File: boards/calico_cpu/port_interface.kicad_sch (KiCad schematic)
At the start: 30 parts, among them J3 Conn_02x06_Top_Bottom, J4 Conn_02x06_Top_Bottom, U58 74HC126, U59 74HC126, U60 74HC126, U61 74HC126, U62 74HC273, U63 74HC273

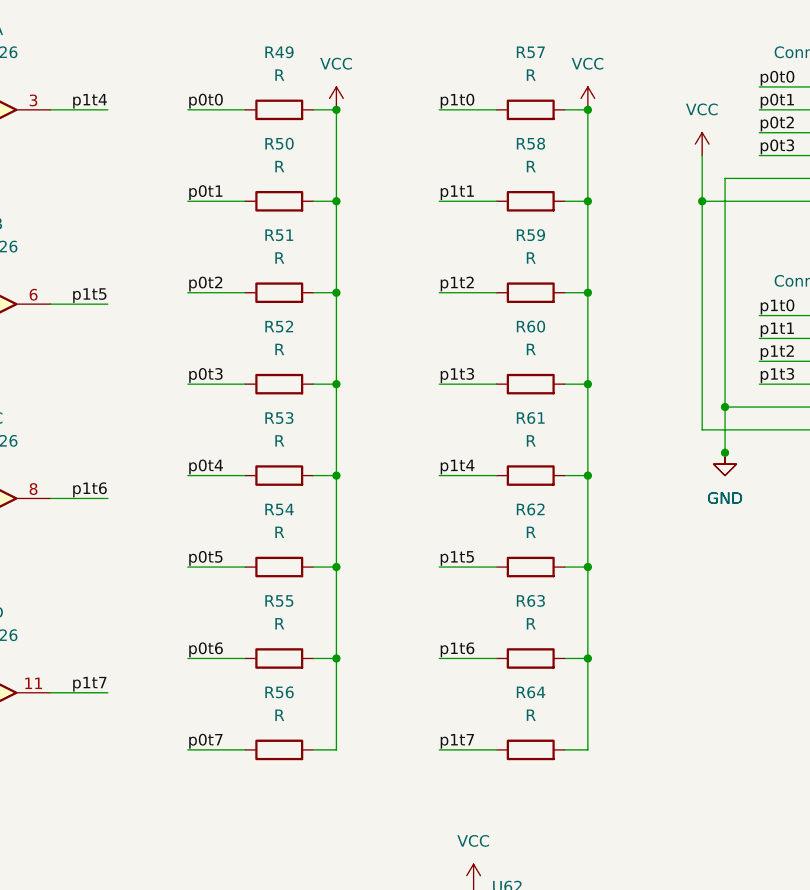
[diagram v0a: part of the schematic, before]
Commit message: set LED and resistors
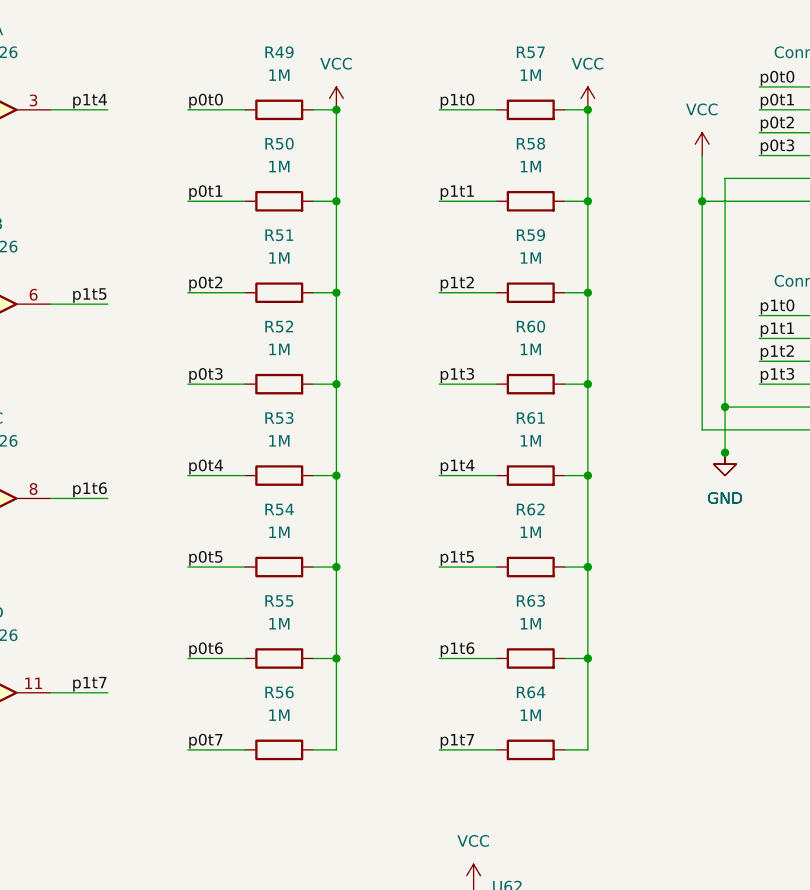
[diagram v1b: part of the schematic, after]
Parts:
- R49, R50, R51, R52, R53, R54, R55, R56, R57, R58, R59, R60, R61, R62, R63, R64: value R -> 1M
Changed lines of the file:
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@@
     (in_bom yes) (on_board yes) (fields_autoplaced)
     (property "Reference" "R57" (id 0) (at 215.9 22.86 90))
-    (property "Value" "R" (id 1) (at 215.9 25.4 90))
+    (property "Value" "1M" (id 1) (at 215.9 25.4 90))
     (property "Footprint" "Resistor_SMD:R_0805_2012Metric_Pad1.20x1.40mm_HandSolder" (id 2) (at 215.9 30.988 90)
       (effects (font (size 1.27 1.27)) hide)
@@
     (in_bom yes) (on_board yes) (fields_autoplaced)
     (property "Reference" "R53" (id 0) (at 187.96 63.5 90))
-    (property "Value" "R" (id 1) (at 187.96 66.04 90))
+    (property "Value" "1M" (id 1) (at 187.96 66.04 90))
     (property "Footprint" "Resistor_SMD:R_0805_2012Metric_Pad1.20x1.40mm_HandSolder" (id 2) (at 187.96 71.628 90)
       (effects (font (size 1.27 1.27)) hide)
@@
     (in_bom yes) (on_board yes) (fields_autoplaced)
     (property "Reference" "R60" (id 0) (at 215.9 53.34 90))
-    (property "Value" "R" (id 1) (at 215.9 55.88 90))
+    (property "Value" "1M" (id 1) (at 215.9 55.88 90))
     (property "Footprint" "Resistor_SMD:R_0805_2012Metric_Pad1.20x1.40mm_HandSolder" (id 2) (at 215.9 61.468 90)
       (effects (font (size 1.27 1.27)) hide)
@@
     (in_bom yes) (on_board yes) (fields_autoplaced)
     (property "Reference" "R49" (id 0) (at 187.96 22.86 90))
-    (property "Value" "R" (id 1) (at 187.96 25.4 90))
+    (property "Value" "1M" (id 1) (at 187.96 25.4 90))
     (property "Footprint" "Resistor_SMD:R_0805_2012Metric_Pad1.20x1.40mm_HandSolder" (id 2) (at 187.96 30.988 90)
       (effects (font (size 1.27 1.27)) hide)
@@
     (in_bom yes) (on_board yes) (fields_autoplaced)
     (property "Reference" "R59" (id 0) (at 215.9 43.18 90))
-    (property "Value" "R" (id 1) (at 215.9 45.72 90))
+    (property "Value" "1M" (id 1) (at 215.9 45.72 90))
     (property "Footprint" "Resistor_SMD:R_0805_2012Metric_Pad1.20x1.40mm_HandSolder" (id 2) (at 215.9 51.308 90)
       (effects (font (size 1.27 1.27)) hide)
@@
     (in_bom yes) (on_board yes) (fields_autoplaced)
     (property "Reference" "R61" (id 0) (at 215.9 63.5 90))
-    (property "Value" "R" (id 1) (at 215.9 66.04 90))
+    (property "Value" "1M" (id 1) (at 215.9 66.04 90))
     (property "Footprint" "Resistor_SMD:R_0805_2012Metric_Pad1.20x1.40mm_HandSolder" (id 2) (at 215.9 71.628 90)
       (effects (font (size 1.27 1.27)) hide)
@@
     (in_bom yes) (on_board yes) (fields_autoplaced)
     (property "Reference" "R62" (id 0) (at 215.9 73.66 90))
-    (property "Value" "R" (id 1) (at 215.9 76.2 90))
+    (property "Value" "1M" (id 1) (at 215.9 76.2 90))
     (property "Footprint" "Resistor_SMD:R_0805_2012Metric_Pad1.20x1.40mm_HandSolder" (id 2) (at 215.9 81.788 90)
       (effects (font (size 1.27 1.27)) hide)
@@
     (in_bom yes) (on_board yes) (fields_autoplaced)
     (property "Reference" "R55" (id 0) (at 187.96 83.82 90))
-    (property "Value" "R" (id 1) (at 187.96 86.36 90))
+    (property "Value" "1M" (id 1) (at 187.96 86.36 90))
     (property "Footprint" "Resistor_SMD:R_0805_2012Metric_Pad1.20x1.40mm_HandSolder" (id 2) (at 187.96 91.948 90)
       (effects (font (size 1.27 1.27)) hide)
@@
     (in_bom yes) (on_board yes) (fields_autoplaced)
     (property "Reference" "R56" (id 0) (at 187.96 93.98 90))
-    (property "Value" "R" (id 1) (at 187.96 96.52 90))
+    (property "Value" "1M" (id 1) (at 187.96 96.52 90))
     (property "Footprint" "Resistor_SMD:R_0805_2012Metric_Pad1.20x1.40mm_HandSolder" (id 2) (at 187.96 102.108 90)
       (effects (font (size 1.27 1.27)) hide)
@@
     (in_bom yes) (on_board yes) (fields_autoplaced)
     (property "Reference" "R52" (id 0) (at 187.96 53.34 90))
-    (property "Value" "R" (id 1) (at 187.96 55.88 90))
+    (property "Value" "1M" (id 1) (at 187.96 55.88 90))
     (property "Footprint" "Resistor_SMD:R_0805_2012Metric_Pad1.20x1.40mm_HandSolder" (id 2) (at 187.96 61.468 90)
       (effects (font (size 1.27 1.27)) hide)
@@
     (in_bom yes) (on_board yes) (fields_autoplaced)
     (property "Reference" "R63" (id 0) (at 215.9 83.82 90))
-    (property "Value" "R" (id 1) (at 215.9 86.36 90))
+    (property "Value" "1M" (id 1) (at 215.9 86.36 90))
     (property "Footprint" "Resistor_SMD:R_0805_2012Metric_Pad1.20x1.40mm_HandSolder" (id 2) (at 215.9 91.948 90)
       (effects (font (size 1.27 1.27)) hide)
@@
     (in_bom yes) (on_board yes) (fields_autoplaced)
     (property "Reference" "R64" (id 0) (at 215.9 93.98 90))
-    (property "Value" "R" (id 1) (at 215.9 96.52 90))
+    (property "Value" "1M" (id 1) (at 215.9 96.52 90))
     (property "Footprint" "Resistor_SMD:R_0805_2012Metric_Pad1.20x1.40mm_HandSolder" (id 2) (at 215.9 102.108 90)
       (effects (font (size 1.27 1.27)) hide)
@@
     (in_bom yes) (on_board yes) (fields_autoplaced)
     (property "Reference" "R51" (id 0) (at 187.96 43.18 90))
-    (property "Value" "R" (id 1) (at 187.96 45.72 90))
+    (property "Value" "1M" (id 1) (at 187.96 45.72 90))
     (property "Footprint" "Resistor_SMD:R_0805_2012Metric_Pad1.20x1.40mm_HandSolder" (id 2) (at 187.96 51.308 90)
       (effects (font (size 1.27 1.27)) hide)
@@
     (in_bom yes) (on_board yes) (fields_autoplaced)
     (property "Reference" "R50" (id 0) (at 187.96 33.02 90))
-    (property "Value" "R" (id 1) (at 187.96 35.56 90))
+    (property "Value" "1M" (id 1) (at 187.96 35.56 90))
     (property "Footprint" "Resistor_SMD:R_0805_2012Metric_Pad1.20x1.40mm_HandSolder" (id 2) (at 187.96 41.148 90)
       (effects (font (size 1.27 1.27)) hide)
@@
     (in_bom yes) (on_board yes) (fields_autoplaced)
     (property "Reference" "R58" (id 0) (at 215.9 33.02 90))
-    (property "Value" "R" (id 1) (at 215.9 35.56 90))
+    (property "Value" "1M" (id 1) (at 215.9 35.56 90))
     (property "Footprint" "Resistor_SMD:R_0805_2012Metric_Pad1.20x1.40mm_HandSolder" (id 2) (at 215.9 41.148 90)
       (effects (font (size 1.27 1.27)) hide)
@@
     (in_bom yes) (on_board yes) (fields_autoplaced)
     (property "Reference" "R54" (id 0) (at 187.96 73.66 90))
-    (property "Value" "R" (id 1) (at 187.96 76.2 90))
+    (property "Value" "1M" (id 1) (at 187.96 76.2 90))
     (property "Footprint" "Resistor_SMD:R_0805_2012Metric_Pad1.20x1.40mm_HandSolder" (id 2) (at 187.96 81.788 90)
       (effects (font (size 1.27 1.27)) hide)

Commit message: unify libraries
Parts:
- J3, J4: footprint PrjLibrary:PinHeader_2x06_P2.54mm_Vertical_Top_Bottom -> ModifiedKiCadLibrary:PinHeader_2x06_P2.54mm_Vertical_Top_Bottom
- U58, U59, U60, U61: footprint PrjLibrary:DIP-14_W7.62mm_D1mm -> ModifiedKiCadLibrary:DIP-14_W7.62mm_D1mm
- U62, U63: footprint PrjLibrary:DIP-20_W7.62mm_D1mm -> ModifiedKiCadLibrary:DIP-20_W7.62mm_D1mm
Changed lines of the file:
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@@
     (property "Reference" "J3" (id 0) (at 254 20.32 0))
     (property "Value" "Conn_02x06_Top_Bottom" (id 1) (at 254 22.86 0))
-    (property "Footprint" "PrjLibrary:PinHeader_2x06_P2.54mm_Vertical_Top_Bottom" (id 2) (at 252.73 31.75 0)
+    (property "Footprint" "ModifiedKiCadLibrary:PinHeader_2x06_P2.54mm_Vertical_Top_Bottom" (id 2) (at 252.73 31.75 0)
       (effects (font (size 1.27 1.27)) hide)
     )
@@
       (effects (font (size 1.27 1.27)) (justify left))
     )
-    (property "Footprint" "PrjLibrary:DIP-14_W7.62mm_D1mm" (id 2) (at 116.84 128.27 0)
+    (property "Footprint" "ModifiedKiCadLibrary:DIP-14_W7.62mm_D1mm" (id 2) (at 116.84 128.27 0)
       (effects (font (size 1.27 1.27)) hide)
     )
@@
     (property "Reference" "U58" (id 0) (at 40.64 41.91 0))
     (property "Value" "74HC126" (id 1) (at 40.64 44.45 0))
-    (property "Footprint" "PrjLibrary:DIP-14_W7.62mm_D1mm" (id 2) (at 40.64 50.8 0)
+    (property "Footprint" "ModifiedKiCadLibrary:DIP-14_W7.62mm_D1mm" (id 2) (at 40.64 50.8 0)
       (effects (font (size 1.27 1.27)) hide)
     )
@@
     (property "Reference" "U60" (id 0) (at 116.84 20.32 0))
     (property "Value" "74HC126" (id 1) (at 116.84 22.86 0))
-    (property "Footprint" "PrjLibrary:DIP-14_W7.62mm_D1mm" (id 2) (at 116.84 29.21 0)
+    (property "Footprint" "ModifiedKiCadLibrary:DIP-14_W7.62mm_D1mm" (id 2) (at 116.84 29.21 0)
       (effects (font (size 1.27 1.27)) hide)
     )
@@
     (property "Reference" "U61" (id 0) (at 154.94 20.32 0))
     (property "Value" "74HC126" (id 1) (at 154.94 22.86 0))
-    (property "Footprint" "PrjLibrary:DIP-14_W7.62mm_D1mm" (id 2) (at 154.94 29.21 0)
+    (property "Footprint" "ModifiedKiCadLibrary:DIP-14_W7.62mm_D1mm" (id 2) (at 154.94 29.21 0)
       (effects (font (size 1.27 1.27)) hide)
     )
@@
     (property "Reference" "U58" (id 0) (at 40.64 63.5 0))
     (property "Value" "74HC126" (id 1) (at 40.64 66.04 0))
-    (property "Footprint" "PrjLibrary:DIP-14_W7.62mm_D1mm" (id 2) (at 40.64 72.39 0)
+    (property "Footprint" "ModifiedKiCadLibrary:DIP-14_W7.62mm_D1mm" (id 2) (at 40.64 72.39 0)
       (effects (font (size 1.27 1.27)) hide)
     )
@@
     (property "Reference" "U58" (id 0) (at 40.64 85.09 0))
     (property "Value" "74HC126" (id 1) (at 40.64 87.63 0))
-    (property "Footprint" "PrjLibrary:DIP-14_W7.62mm_D1mm" (id 2) (at 40.64 93.98 0)
+    (property "Footprint" "ModifiedKiCadLibrary:DIP-14_W7.62mm_D1mm" (id 2) (at 40.64 93.98 0)
       (effects (font (size 1.27 1.27)) hide)
     )
@@
     (property "Reference" "U59" (id 0) (at 78.74 20.32 0))
     (property "Value" "74HC126" (id 1) (at 78.74 22.86 0))
-    (property "Footprint" "PrjLibrary:DIP-14_W7.62mm_D1mm" (id 2) (at 78.74 29.21 0)
+    (property "Footprint" "ModifiedKiCadLibrary:DIP-14_W7.62mm_D1mm" (id 2) (at 78.74 29.21 0)
       (effects (font (size 1.27 1.27)) hide)
     )
@@
     (property "Reference" "U60" (id 0) (at 116.84 85.09 0))
     (property "Value" "74HC126" (id 1) (at 116.84 87.63 0))
-    (property "Footprint" "PrjLibrary:DIP-14_W7.62mm_D1mm" (id 2) (at 116.84 93.98 0)
+    (property "Footprint" "ModifiedKiCadLibrary:DIP-14_W7.62mm_D1mm" (id 2) (at 116.84 93.98 0)
       (effects (font (size 1.27 1.27)) hide)
     )
@@
     (property "Reference" "U59" (id 0) (at 78.74 85.09 0))
     (property "Value" "74HC126" (id 1) (at 78.74 87.63 0))
-    (property "Footprint" "PrjLibrary:DIP-14_W7.62mm_D1mm" (id 2) (at 78.74 93.98 0)
+    (property "Footprint" "ModifiedKiCadLibrary:DIP-14_W7.62mm_D1mm" (id 2) (at 78.74 93.98 0)
       (effects (font (size 1.27 1.27)) hide)
     )
@@
     (property "Reference" "J4" (id 0) (at 254 45.72 0))
     (property "Value" "Conn_02x06_Top_Bottom" (id 1) (at 254 48.26 0))
-    (property "Footprint" "PrjLibrary:PinHeader_2x06_P2.54mm_Vertical_Top_Bottom" (id 2) (at 252.73 57.15 0)
+    (property "Footprint" "ModifiedKiCadLibrary:PinHeader_2x06_P2.54mm_Vertical_Top_Bottom" (id 2) (at 252.73 57.15 0)
       (effects (font (size 1.27 1.27)) hide)
     )
@@
     (property "Reference" "U59" (id 0) (at 78.74 63.5 0))
     (property "Value" "74HC126" (id 1) (at 78.74 66.04 0))
-    (property "Footprint" "PrjLibrary:DIP-14_W7.62mm_D1mm" (id 2) (at 78.74 72.39 0)
+    (property "Footprint" "ModifiedKiCadLibrary:DIP-14_W7.62mm_D1mm" (id 2) (at 78.74 72.39 0)
       (effects (font (size 1.27 1.27)) hide)
     )
@@
     (property "Reference" "U61" (id 0) (at 154.94 41.91 0))
     (property "Value" "74HC126" (id 1) (at 154.94 44.45 0))
-    (property "Footprint" "PrjLibrary:DIP-14_W7.62mm_D1mm" (id 2) (at 154.94 50.8 0)
+    (property "Footprint" "ModifiedKiCadLibrary:DIP-14_W7.62mm_D1mm" (id 2) (at 154.94 50.8 0)
       (effects (font (size 1.27 1.27)) hide)
     )
@@
       (effects (font (size 1.27 1.27)) (justify left))
     )
-    (property "Footprint" "PrjLibrary:DIP-20_W7.62mm_D1mm" (id 2) (at 209.55 135.89 0)
+    (property "Footprint" "ModifiedKiCadLibrary:DIP-20_W7.62mm_D1mm" (id 2) (at 209.55 135.89 0)
       (effects (font (size 1.27 1.27)) hide)
     )
@@
       (effects (font (size 1.27 1.27)) (justify left))
     )
-    (property "Footprint" "PrjLibrary:DIP-14_W7.62mm_D1mm" (id 2) (at 154.94 128.27 0)
+    (property "Footprint" "ModifiedKiCadLibrary:DIP-14_W7.62mm_D1mm" (id 2) (at 154.94 128.27 0)
       (effects (font (size 1.27 1.27)) hide)
     )
@@
     (property "Reference" "U59" (id 0) (at 78.74 41.91 0))
     (property "Value" "74HC126" (id 1) (at 78.74 44.45 0))
-    (property "Footprint" "PrjLibrary:DIP-14_W7.62mm_D1mm" (id 2) (at 78.74 50.8 0)
+    (property "Footprint" "ModifiedKiCadLibrary:DIP-14_W7.62mm_D1mm" (id 2) (at 78.74 50.8 0)
       (effects (font (size 1.27 1.27)) hide)
     )
@@
     (property "Reference" "U58" (id 0) (at 40.64 20.32 0))
     (property "Value" "74HC126" (id 1) (at 40.64 22.86 0))
-    (property "Footprint" "PrjLibrary:DIP-14_W7.62mm_D1mm" (id 2) (at 40.64 29.21 0)
+    (property "Footprint" "ModifiedKiCadLibrary:DIP-14_W7.62mm_D1mm" (id 2) (at 40.64 29.21 0)
       (effects (font (size 1.27 1.27)) hide)
     )
@@
     (property "Reference" "U61" (id 0) (at 154.94 85.09 0))
     (property "Value" "74HC126" (id 1) (at 154.94 87.63 0))
-    (property "Footprint" "PrjLibrary:DIP-14_W7.62mm_D1mm" (id 2) (at 154.94 93.98 0)
+    (property "Footprint" "ModifiedKiCadLibrary:DIP-14_W7.62mm_D1mm" (id 2) (at 154.94 93.98 0)
       (effects (font (size 1.27 1.27)) hide)
     )
@@
     (property "Reference" "U60" (id 0) (at 116.84 41.91 0))
     (property "Value" "74HC126" (id 1) (at 116.84 44.45 0))
-    (property "Footprint" "PrjLibrary:DIP-14_W7.62mm_D1mm" (id 2) (at 116.84 50.8 0)
+    (property "Footprint" "ModifiedKiCadLibrary:DIP-14_W7.62mm_D1mm" (id 2) (at 116.84 50.8 0)
       (effects (font (size 1.27 1.27)) hide)
     )
@@
       (effects (font (size 1.27 1.27)) (justify left))
     )
-    (property "Footprint" "PrjLibrary:DIP-20_W7.62mm_D1mm" (id 2) (at 254 135.89 0)
+    (property "Footprint" "ModifiedKiCadLibrary:DIP-20_W7.62mm_D1mm" (id 2) (at 254 135.89 0)
       (effects (font (size 1.27 1.27)) hide)
     )
@@
     (property "Reference" "U61" (id 0) (at 154.94 63.5 0))
     (property "Value" "74HC126" (id 1) (at 154.94 66.04 0))
-    (property "Footprint" "PrjLibrary:DIP-14_W7.62mm_D1mm" (id 2) (at 154.94 72.39 0)
+    (property "Footprint" "ModifiedKiCadLibrary:DIP-14_W7.62mm_D1mm" (id 2) (at 154.94 72.39 0)
       (effects (font (size 1.27 1.27)) hide)
     )
@@
       (effects (font (size 1.27 1.27)) (justify left))
     )
-    (property "Footprint" "PrjLibrary:DIP-14_W7.62mm_D1mm" (id 2) (at 40.64 128.27 0)
+    (property "Footprint" "ModifiedKiCadLibrary:DIP-14_W7.62mm_D1mm" (id 2) (at 40.64 128.27 0)
       (effects (font (size 1.27 1.27)) hide)
     )
@@
       (effects (font (size 1.27 1.27)) (justify left))
     )
-    (property "Footprint" "PrjLibrary:DIP-14_W7.62mm_D1mm" (id 2) (at 78.74 128.27 0)
+    (property "Footprint" "ModifiedKiCadLibrary:DIP-14_W7.62mm_D1mm" (id 2) (at 78.74 128.27 0)
       (effects (font (size 1.27 1.27)) hide)
     )
@@
     (property "Reference" "U60" (id 0) (at 116.84 63.5 0))
     (property "Value" "74HC126" (id 1) (at 116.84 66.04 0))
-    (property "Footprint" "PrjLibrary:DIP-14_W7.62mm_D1mm" (id 2) (at 116.84 72.39 0)
-      (effects (font (size 1.27 1.27)) hide)
-    )
+    (property "Footprint" "ModifiedKiCadLibrary:DIP-14_W7.62mm_D1mm" (id 2) (at 116.84 72.39 0)
+      (effects (font (size 1.27 1.27)) hide)
+    )
